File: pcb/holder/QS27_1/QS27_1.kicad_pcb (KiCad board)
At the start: 2 copper layers, 229.9 x 64.9 mm, 21 parts, among them J1 Conn_01x10, J2 Conn_01x10, J3 Conn_01x10, J4 Conn_01x10, J5 Conn_01x03, Q1 MPSA42, U1 NE555P

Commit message: Fix nixie pin assignment
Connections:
- NX1 pad 1: Net-(J1-Pad10) -> Net-(J1-Pad2)
- NX1 pad 2: Net-(J1-Pad9) -> Net-(J1-Pad3)
- NX1 pad 3: Net-(J1-Pad8) -> Net-(J1-Pad4)
- NX1 pad 4: Net-(J1-Pad7) -> Net-(J1-Pad5)
- NX1 pad 6: Net-(J1-Pad5) -> Net-(J1-Pad7)
- NX1 pad 7: Net-(J1-Pad4) -> Net-(J1-Pad8)
- NX1 pad 8: Net-(J1-Pad3) -> Net-(J1-Pad9)
- NX1 pad 9: Net-(J1-Pad2) -> Net-(J1-Pad10)
- NX2 pad 1: Net-(J2-Pad10) -> Net-(J2-Pad2)
- NX2 pad 2: Net-(J2-Pad9) -> Net-(J2-Pad3)
- NX2 pad 3: Net-(J2-Pad8) -> Net-(J2-Pad4)
- NX2 pad 4: Net-(J2-Pad7) -> Net-(J2-Pad5)
- NX2 pad 6: Net-(J2-Pad5) -> Net-(J2-Pad7)
- NX2 pad 7: Net-(J2-Pad4) -> Net-(J2-Pad8)
- NX2 pad 8: Net-(J2-Pad3) -> Net-(J2-Pad9)
- NX2 pad 9: Net-(J2-Pad2) -> Net-(J2-Pad10)
- NX3 pad 1: Net-(J3-Pad10) -> Net-(J3-Pad2)
- NX3 pad 2: Net-(J3-Pad9) -> Net-(J3-Pad3)
- NX3 pad 3: Net-(J3-Pad8) -> Net-(J3-Pad4)
- NX3 pad 4: Net-(J3-Pad7) -> Net-(J3-Pad5)
- NX3 pad 6: Net-(J3-Pad5) -> Net-(J3-Pad7)
- NX3 pad 7: Net-(J3-Pad4) -> Net-(J3-Pad8)
- NX3 pad 8: Net-(J3-Pad3) -> Net-(J3-Pad9)
- NX3 pad 9: Net-(J3-Pad2) -> Net-(J3-Pad10)
- NX4 pad 1: Net-(J4-Pad10) -> Net-(J4-Pad2)
- NX4 pad 2: Net-(J4-Pad9) -> Net-(J4-Pad3)
- NX4 pad 3: Net-(J4-Pad8) -> Net-(J4-Pad4)
- NX4 pad 4: Net-(J4-Pad7) -> Net-(J4-Pad5)
- NX4 pad 6: Net-(J4-Pad5) -> Net-(J4-Pad7)
- NX4 pad 7: Net-(J4-Pad4) -> Net-(J4-Pad8)
- NX4 pad 8: Net-(J4-Pad3) -> Net-(J4-Pad9)
- NX4 pad 9: Net-(J4-Pad2) -> Net-(J4-Pad10)
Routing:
- net Net-(J1-Pad3): track 31.7 -> 46.6 mm
- net Net-(J3-Pad3): track 27.3 -> 41.9 mm
- net Net-(J1-Pad4): track 28.3 -> 42.0 mm
- net Net-(J2-Pad2): track 29.3 -> 42.0 mm
- net Net-(J3-Pad4): track 23.8 -> 36.5 mm
- net Net-(J3-Pad2): track 31.8 -> 44.4 mm
- net Net-(J1-Pad2): track 36.3 -> 48.9 mm
- net Net-(J1-Pad8): track 35.3 -> 24.1 mm
- net Net-(J1-Pad5): track 27.4 -> 38.2 mm
- net Net-(J1-Pad10): track 42.2 -> 31.7 mm
- net Net-(J4-Pad8): track 34.5 -> 44.8 mm
- net Net-(J1-Pad9): track 38.4 -> 28.6 mm
- net Net-(J2-Pad4): track 22.9 -> 32.0 mm
- net Net-(J4-Pad7): track 30.0 -> 38.9 mm
- net Net-(J3-Pad5): track 23.0 -> 31.9 mm
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
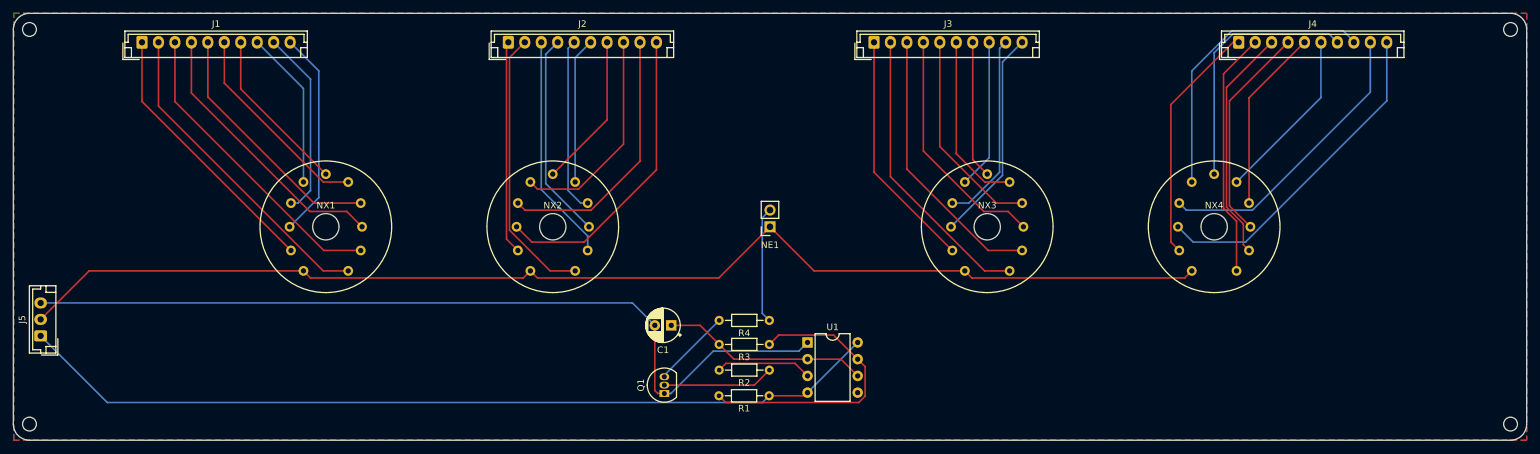
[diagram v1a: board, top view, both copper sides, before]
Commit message: Fix layout errors
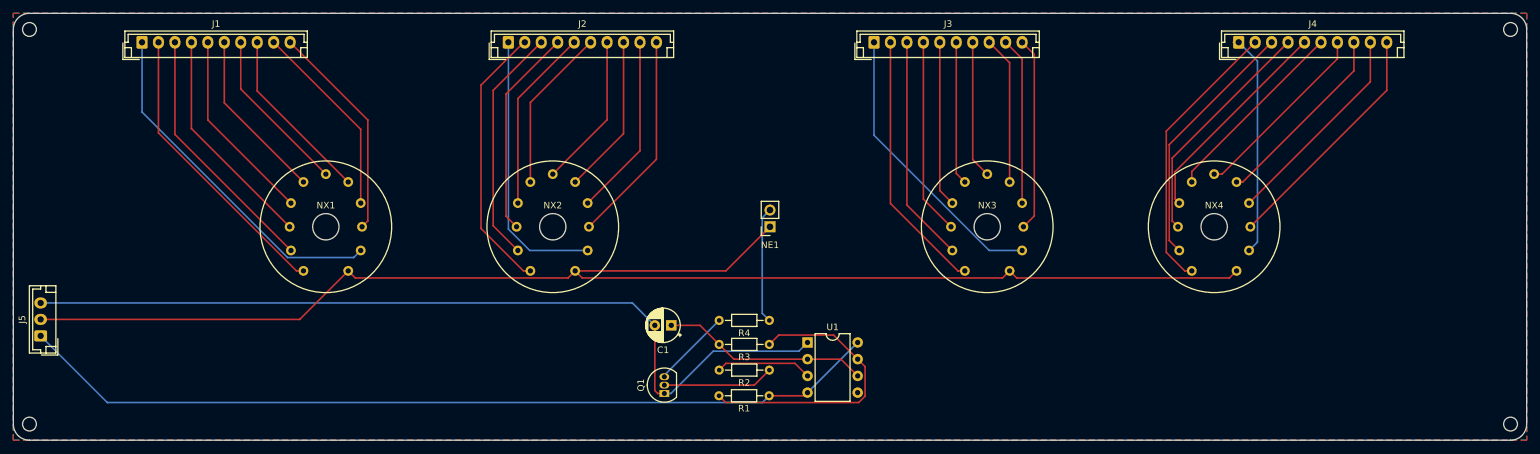
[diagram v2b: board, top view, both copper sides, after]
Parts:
- R4: value 50k -> 100k
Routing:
- net ANODE_PIN: track 186.2 -> 220.2 mm
- net Net-(J4-Pad8): track 44.8 -> 29.3 mm
- net Net-(J4-Pad10): track 50.5 -> 36.6 mm
- net Net-(J2-Pad10): track 46.1 -> 32.3 mm
- net Net-(J4-Pad9): track 44.5 -> 32.1 mm
- net Net-(J1-Pad1): track 41.0 -> 53.4 mm
- net Net-(J2-Pad9): track 40.1 -> 28.0 mm
- net Net-(J4-Pad7): track 38.9 -> 28.5 mm
- net Net-(J2-Pad1): track 32.6 -> 42.3 mm
- net Net-(J2-Pad8): track 32.9 -> 24.3 mm
- net Net-(J1-Pad5): track 38.2 -> 29.7 mm
- net Net-(J1-Pad4): track 42.0 -> 34.2 mm
- net Net-(J1-Pad3): track 46.6 -> 38.9 mm
- net Net-(J3-Pad3): track 41.9 -> 34.5 mm
- net Net-(J3-Pad1): track 36.6 -> 43.9 mm
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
